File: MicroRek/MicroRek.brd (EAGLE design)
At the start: 40 x 30 mm, 18 parts, among them IC3 LSM9DS1TR

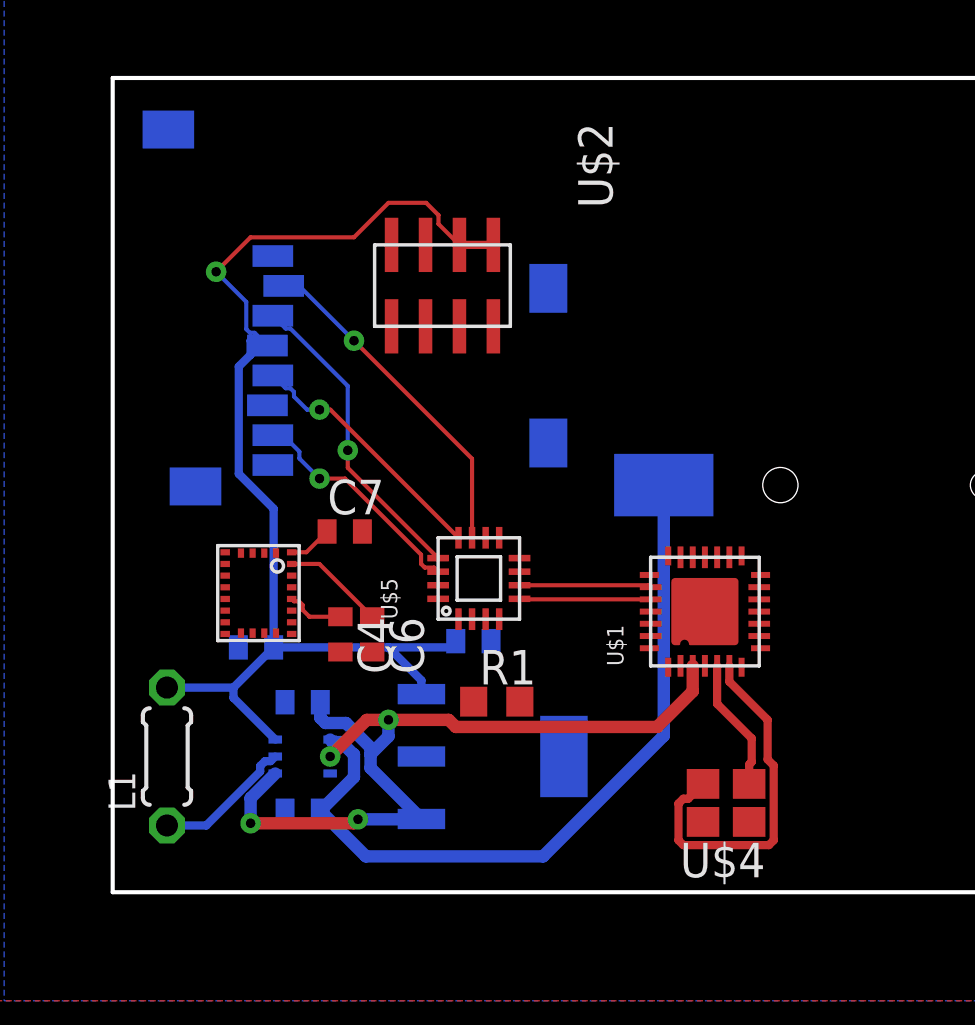
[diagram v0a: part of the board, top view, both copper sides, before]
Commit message: Rewiring on Microrek
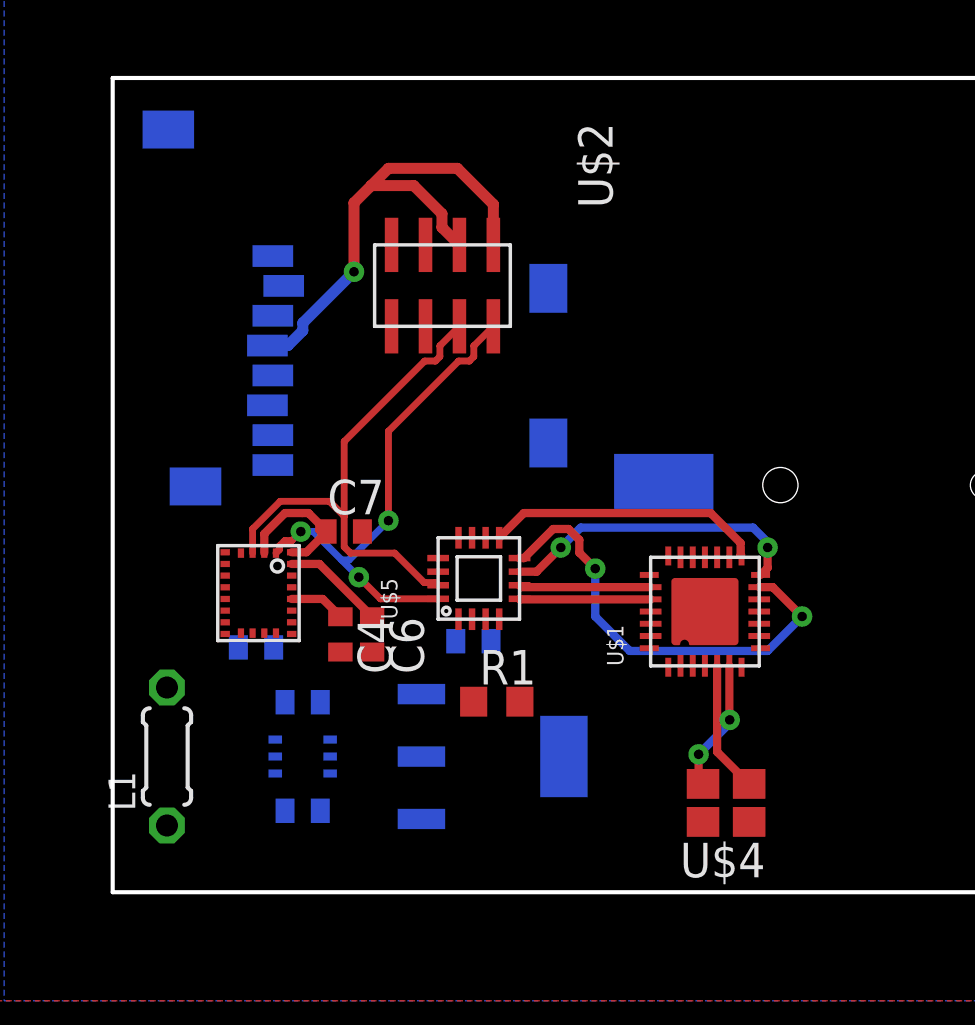
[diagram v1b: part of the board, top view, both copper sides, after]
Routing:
- net 5V: track 31.9 -> 0.00 mm, vias 4 -> 0
- net N$2: track 28.1 -> 0.00 mm
- net 3.3V: track 44.5 -> 19.2 mm
- net SDA3: track 0.00 -> 19.1 mm
- net SCL3: track 0.00 -> 18.7 mm, vias 0 -> 3
- net MOSI5: track 0.00 -> 16.6 mm, vias 0 -> 2
- net D23: track 12.5 -> 0.00 mm, vias 1 -> 0
- net MOSI3: track 11.6 -> 0.00 mm, vias 1 -> 0
- net MISO5: track 0.00 -> 11.4 mm, vias 0 -> 2
- net SCK5: track 0.00 -> 10.2 mm
- net SCK3: track 9.42 -> 0.00 mm, vias 1 -> 0
- net MISO3: track 8.52 -> 0.00 mm, vias 1 -> 0
- net CPB7: track 13.3 -> 4.90 mm, vias 0 -> 2
- net N$3: track 5.16 -> 0.00 mm
- net N$7: track 1.62 -> 5.38 mm

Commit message: Updated MicroRek Board Layout
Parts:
- moved C4 0.13 mm to (8.26, 9.50)
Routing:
- net 3.3V: track 19.2 -> 47.3 mm, vias 1 -> 3
- net 5V: track 0.00 -> 24.8 mm, vias 0 -> 1
- net N$2: track 0.00 -> 22.4 mm, vias 0 -> 2
- net MOSI3: track 0.00 -> 21.5 mm, vias 0 -> 1
- net D23: track 0.00 -> 14.3 mm, vias 0 -> 3
- net SDA3: track 19.1 -> 31.7 mm, vias 0 -> 2
- net SCK3: track 0.00 -> 9.60 mm, vias 0 -> 1
- net MISO3: track 0.00 -> 9.31 mm, vias 0 -> 1
- net N$3: track 0.00 -> 5.04 mm
- net SCL3: track 18.7 -> 22.8 mm, vias 3 -> 5
